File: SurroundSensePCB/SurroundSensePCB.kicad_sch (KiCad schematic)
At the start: 31 parts, among them J1 out_positive, J2 out_negative, J3 VIN, J4 GND_IN, U1 2.4GHz

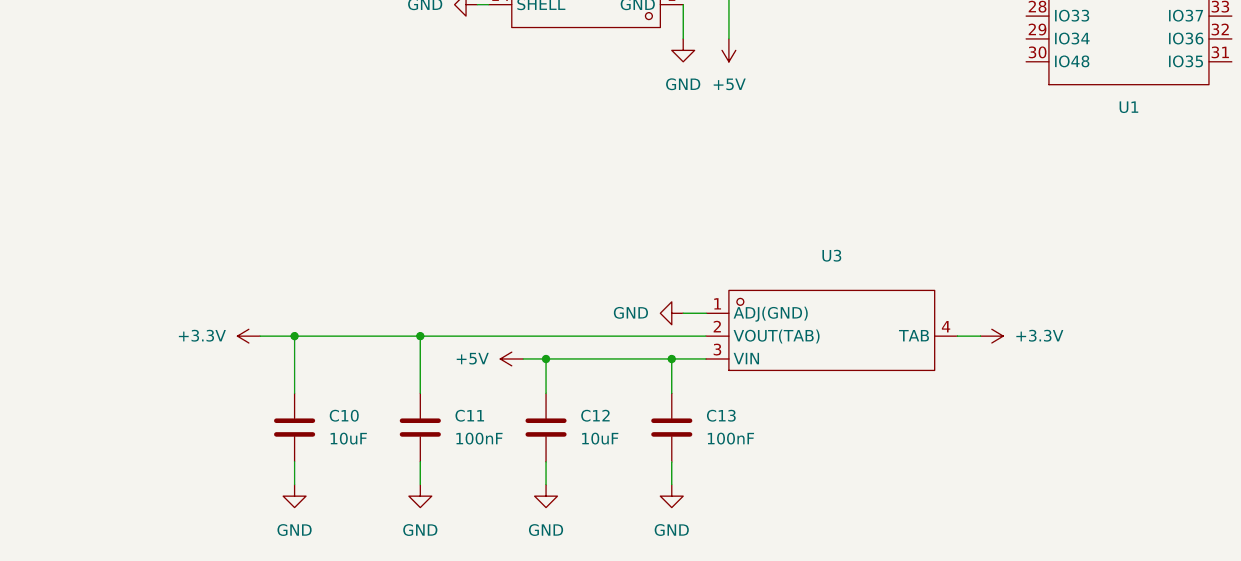
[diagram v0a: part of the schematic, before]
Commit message: parts selected, ordered
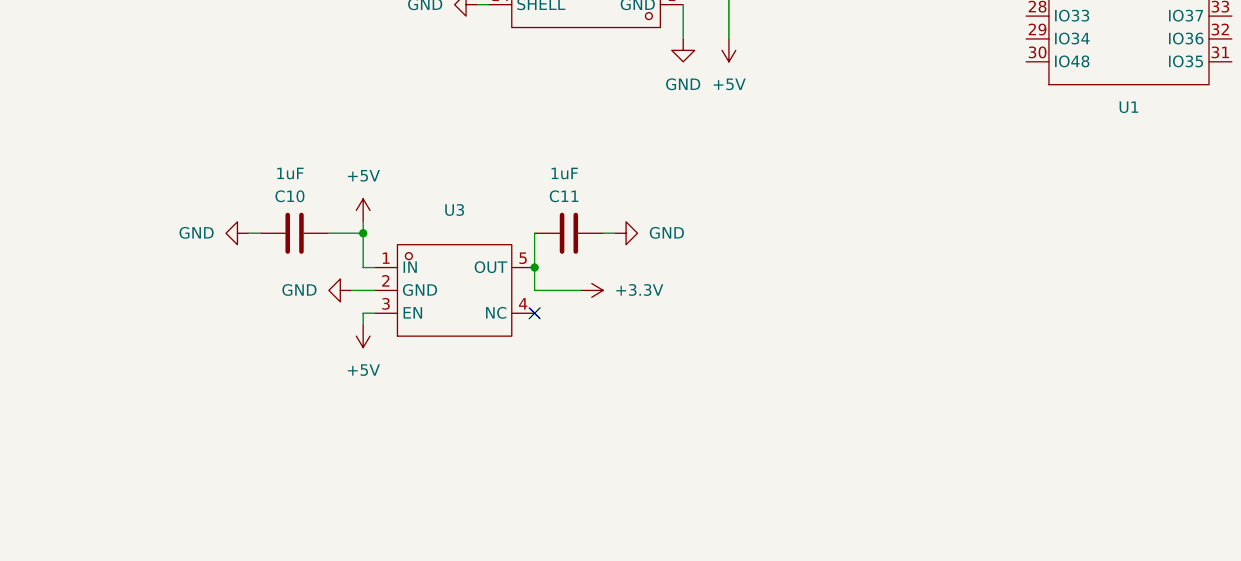
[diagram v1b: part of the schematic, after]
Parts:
- removed C12: 10uF, Capacitor_SMD:C_0402_1005Metric, symbol Device:C
- removed C13: 100nF, Capacitor_SMD:C_0402_1005Metric, symbol Device:C
- removed U3: ~, AMS1117-3.3:SOT-223-4_L6.5-W3.5-P2.30-LS7.0-BR, symbol AMS1117-3.3:AMS1117-3.3_C347222
- added U3: ~, TLV75533PDBVR:SOT-23-5_L3.0-W1.7-P0.95-LS2.8-BR, symbol TLV75533PDBVR:TLV75533PDBVR
- C10: value 10uF -> 1uF
- C11: value 100nF -> 1uF
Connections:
- net +3.3V: now also U3.5 (OUT); no longer C10.1
- net +5V: now also C10.2, U3.1 (IN), U3.3 (EN)
- net GND: now also C10.1, U3.2 (GND); no longer C10.2
- no-connect marks 0 -> 1
